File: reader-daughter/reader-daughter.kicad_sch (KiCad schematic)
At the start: 24 parts, among them J1 Conn_01x10_Female, J2 Conn_01x10_Female, J3 Conn_01x03_Male, J4 Conn_01x03_Female, J5 Conn_01x19_Female, J6 Conn_01x19_Female, J7 Conn_01x08_Male, T1 AO3400A

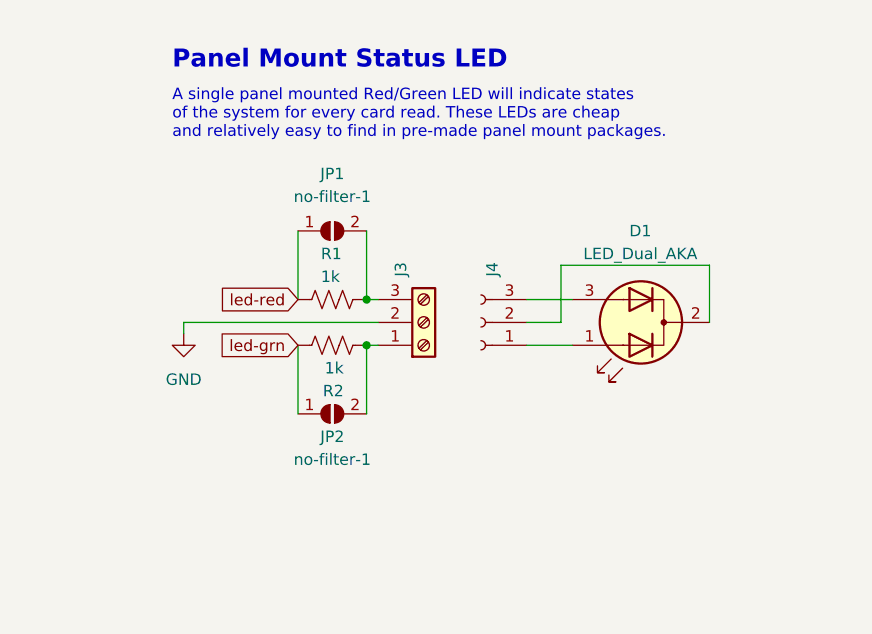
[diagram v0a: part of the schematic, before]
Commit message: updated boards with improved silkscreen and pad-shapes
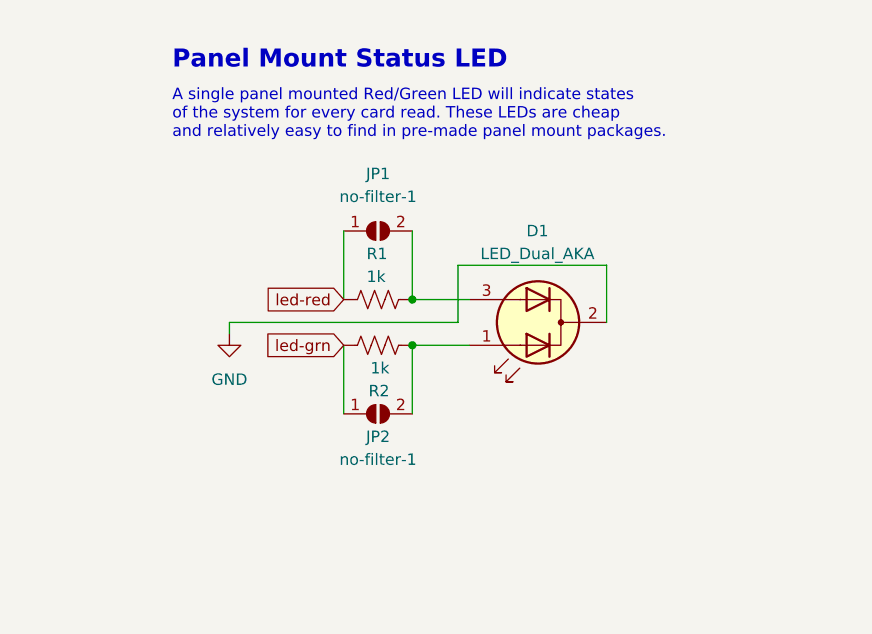
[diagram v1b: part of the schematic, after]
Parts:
- removed J3: Conn_01x03_Male, TerminalBlock_TE-Connectivity:TerminalBlock_TE_282834-3_1x03_P2.54mm_Horizontal, symbol Connector:Screw_Terminal_01x03
- removed J4: Conn_01x03_Female, symbol Connector:Conn_01x03_Female
- D1: footprint (none) -> LED_THT:LED_D5.0mm-3
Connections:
- net GND: now also D1.2 (K)
- net at JP1.2 (B), R1.2: now also D1.3 (A2)
- net at JP2.2 (B), R2.1: now also D1.1 (A1)
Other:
- moved on the sheet: D1, JP1, JP2, R1, R2
